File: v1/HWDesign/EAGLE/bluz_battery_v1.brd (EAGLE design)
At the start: 20.3 x 58.4 mm, 11 parts, among them Q1 NTS2101PT1G

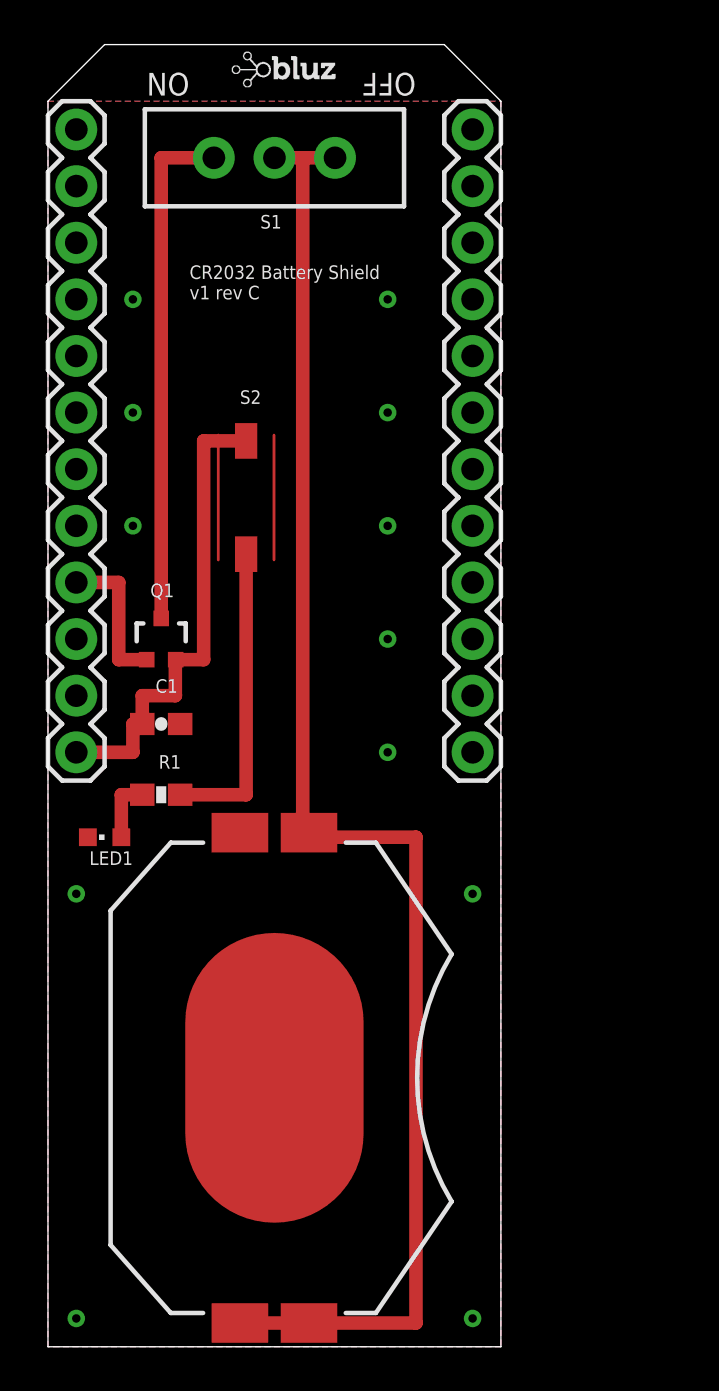
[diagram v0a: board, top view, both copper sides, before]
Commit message: changed battery shield to have breakouts and moved switch
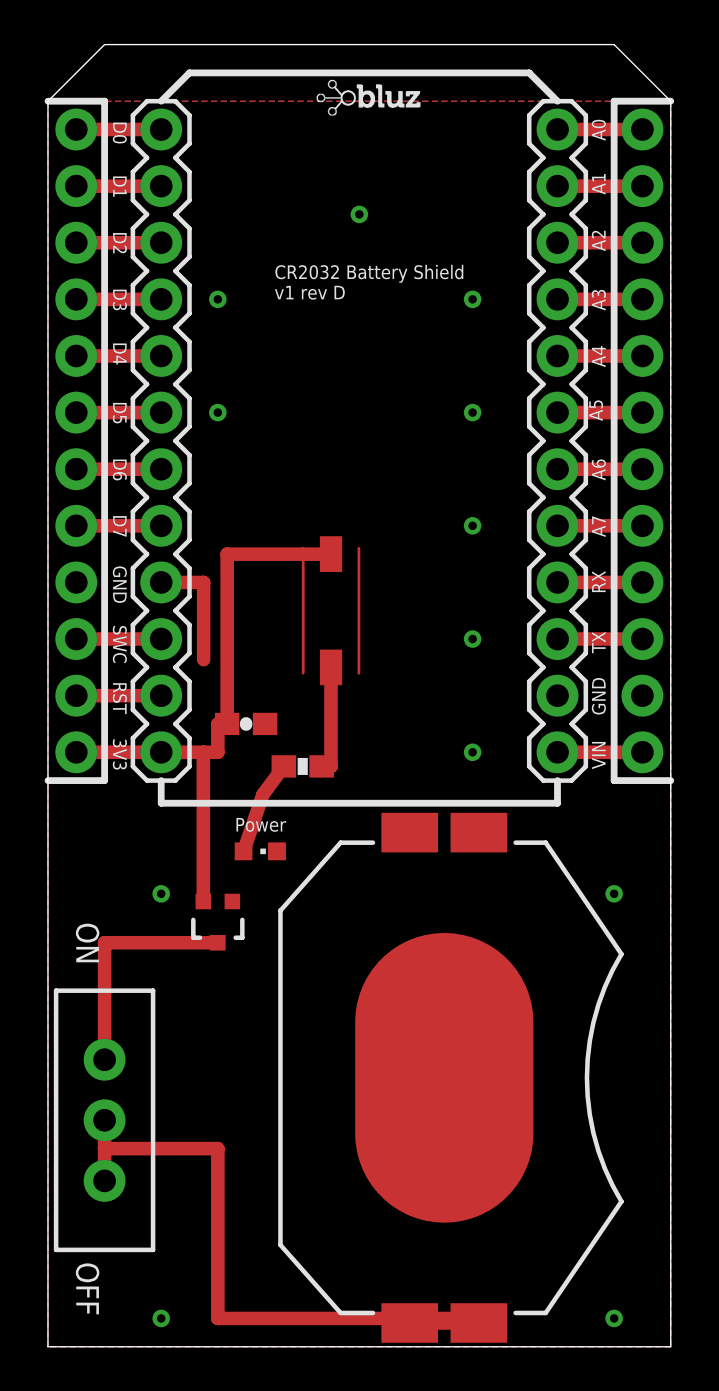
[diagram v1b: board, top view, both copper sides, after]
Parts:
- added JP1, JP4: M121X12_NO_SILK_KIT, SparkFun-Connectors:1X12_NO_SILK_KIT
- moved S1 43.8 mm to (2.54, 10.2), turned to 0 degrees
- moved Q1 13.0 mm to (7.62, 19.1), turned to 180 degrees
- moved BAT1 7.62 mm to (17.8, 12.1)
- moved LED1 7.01 mm to (9.53, 22.2), turned to 270 degrees
- moved R1 6.48 mm to (11.4, 26.0)
- moved S2 6.35 mm to (12.7, 33.0)
- moved U$1 4.02 mm to (12.1, 55.2)
- moved C1 3.81 mm to (8.89, 27.9)
- moved JP2 3.81 mm to (5.08, 54.6)
- moved JP3 3.81 mm to (22.9, 54.6)
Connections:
- new net N$10: JP1.6, JP3.6
- new net N$11: JP1.7, JP3.7
- new net N$12: JP1.8, JP3.8
- new net N$13: JP1.9, JP3.9
- new net N$14: JP1.10, JP3.10
- new net N$16: JP1.12, JP3.12
- new net N$17: JP2.1, JP4.1
- new net N$18: JP2.2, JP4.2
- new net N$19: JP2.3, JP4.3
- new net N$2: JP1.1, JP3.1
- new net N$20: JP2.4, JP4.4
- new net N$21: JP2.5, JP4.5
- new net N$22: JP2.6, JP4.6
- new net N$23: JP2.7, JP4.7
- new net N$24: JP2.8, JP4.8
- new net N$25: JP2.10, JP4.10
- new net N$26: JP2.11, JP4.11
- new net N$6: JP1.2, JP3.2
- new net N$7: JP1.3, JP3.3
- new net N$8: JP1.4, JP3.4
- new net N$9: JP1.5, JP3.5
- net GND: now also JP1.11, JP3.11, JP4.9
- net VCC: now also JP4.12
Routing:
- net N$1: track 68.0 -> 31.1 mm
- net N$5: track 23.0 -> 10.3 mm
- net N$4: track 13.8 -> 4.87 mm
- net VCC: track 21.6 -> 27.0 mm
- net N$9: track 0.00 -> 3.81 mm
- net N$8: track 0.00 -> 3.81 mm
- net N$7: track 0.00 -> 3.81 mm
- net N$6: track 0.00 -> 3.81 mm
- net N$2: track 0.00 -> 3.81 mm
- net N$16: track 0.00 -> 3.81 mm
- net N$14: track 0.00 -> 3.81 mm
- net N$13: track 0.00 -> 3.81 mm
- net N$12: track 0.00 -> 3.81 mm
- net N$11: track 0.00 -> 3.81 mm
- net N$10: track 0.00 -> 3.81 mm
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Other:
- board size 20.3 x 58.4 mm -> 27.9 x 58.4 mm
- board text added: "3V3"
- board text added: "A0"
- board text added: "A1"
- board text added: "A2"
- board text added: "A3"
- board text added: "A4"
- board text added: "A5"
- board text added: "A6"
- board text added: "A7"
- board text added: "CR2032 Battery Shield v1 rev D"
- board text added: "D0"
- board text added: "D1"
- board text added: "D2"
- board text added: "D3"
- board text added: "D4"
- board text added: "D5"
- board text added: "D6"
- board text added: "D7"
- board text added: "GND"
- board text added: "Power"
- board text added: "RST"
- board text added: "RX"
- board text added: "SWC"
- board text added: "TX"
- board text added: "VIN"
- board text removed: "CR2032 Battery Shield v1 rev C"

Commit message: updated slightly
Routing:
- net VCC: track 27.0 -> 32.1 mm
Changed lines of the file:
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@@
 <wire x1="2.54" y1="58.42" x2="0" y2="55.88" width="0" layer="20"/>
 <wire x1="0" y1="55.88" x2="0" y2="0" width="0" layer="20"/>
-<text x="10.16" y="46.99" size="0.6096" layer="21">CR2032 Battery Shield
+<text x="7.62" y="43.18" size="0.8128" layer="21">CR2032 Battery Shield
 v1 rev D</text>
 <text x="1.27" y="19.05" size="1.016" layer="21" rot="SR270">ON</text>
@@
 <wire x1="6.97" y1="19.975" x2="6.97" y2="26.67" width="0.6096" layer="1"/>
 <wire x1="6.97" y1="26.67" x2="7.62" y2="26.67" width="0.6096" layer="1"/>
-<wire x1="8.04" y1="27.94" x2="8.04" y2="35.56" width="0.6096" layer="1"/>
-<wire x1="8.04" y1="35.56" x2="12.7" y2="35.56" width="0.6096" layer="1"/>
+<wire x1="8.04" y1="27.94" x2="8.04" y2="38.1" width="0.6096" layer="1"/>
 <contactref element="JP4" pad="12"/>
 <wire x1="1.27" y1="26.67" x2="5.08" y2="26.67" width="0.6096" layer="1"/>
+<wire x1="8.04" y1="38.1" x2="12.7" y2="38.1" width="0.6096" layer="1"/>
+<wire x1="12.7" y1="38.1" x2="12.7" y2="35.56" width="0.6096" layer="1"/>
 </signal>
 <signal name="N$3">
